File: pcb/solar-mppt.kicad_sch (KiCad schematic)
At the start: 2 parts, among them U1 BQ25798, U2 STM32G491KEUx

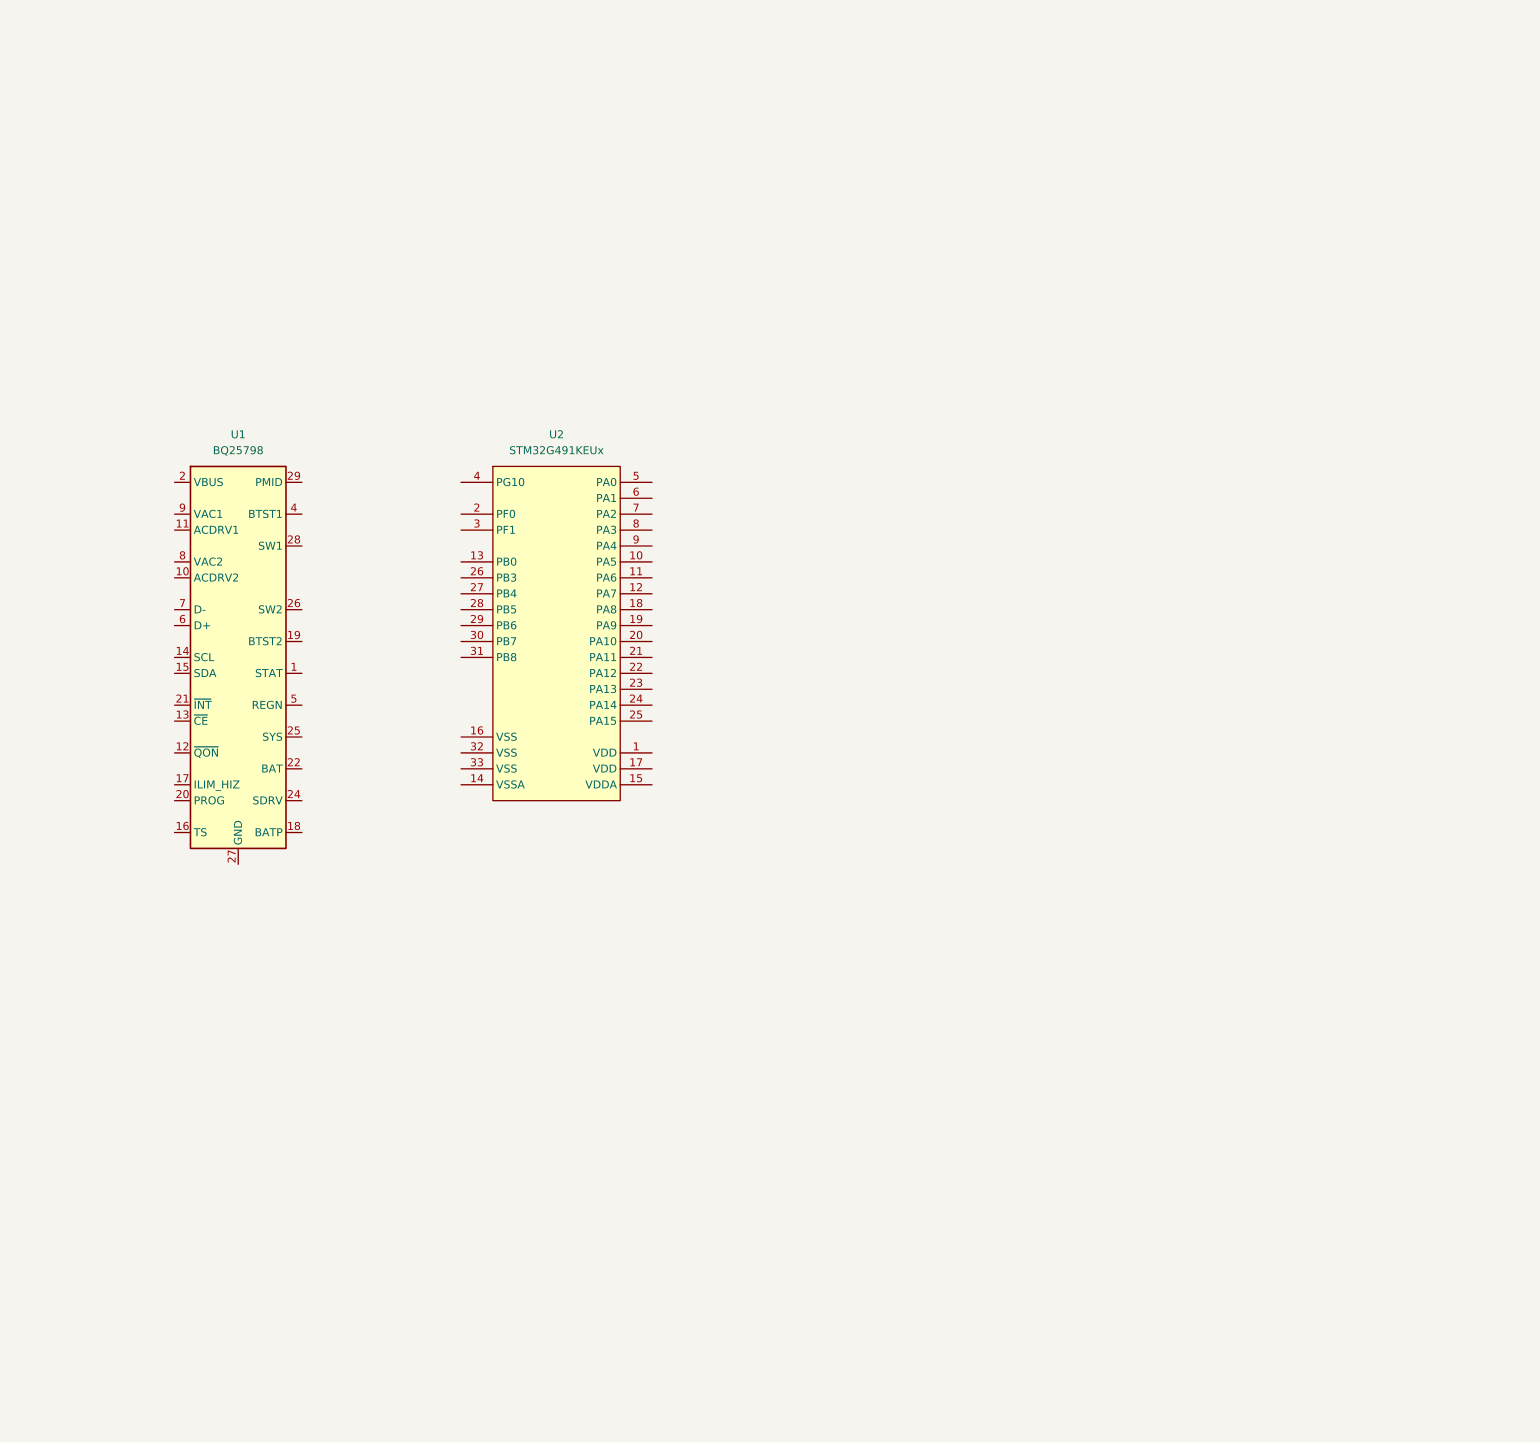
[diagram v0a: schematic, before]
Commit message: mppt vac/acdrv/vbus reverse protection b2b nmos
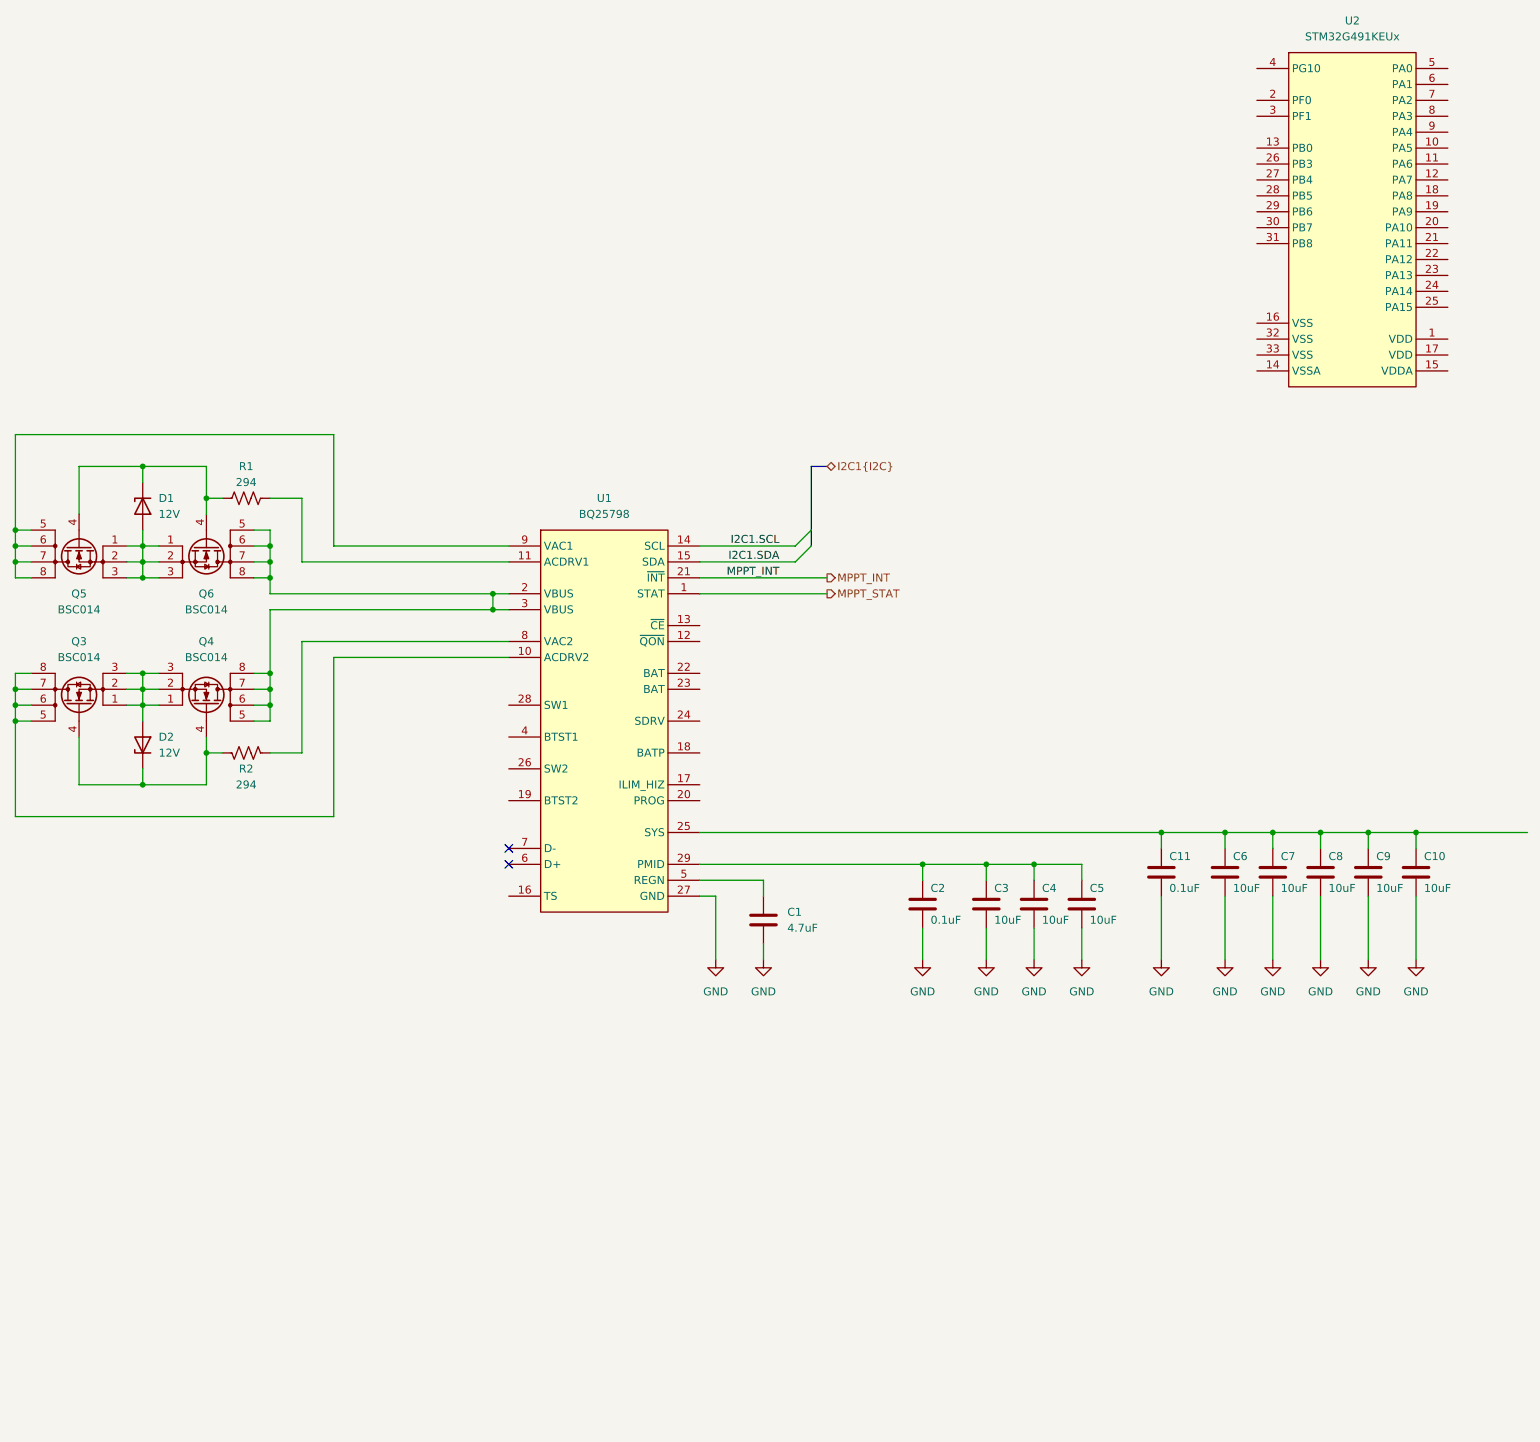
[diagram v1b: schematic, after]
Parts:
- added C1: 4.7uF, Capacitor_SMD:C_0402_1005Metric, symbol Device:C
- added C10, C3, C4, C5, C6, C7, C8, C9: 10uF, Capacitor_SMD:C_0402_1005Metric, symbol Device:C
- added C11, C2: 0.1uF, Capacitor_SMD:C_0402_1005Metric, symbol Device:C
- added D1, D2: 12V, symbol Device:D_Zener
- added Q3, Q4, Q5, Q6: BSC014, symbol Transistor_FET:Q_NMOS_DGS
- added R1, R2: 294, Resistor_SMD:R_0402_1005Metric, symbol Device:R_US
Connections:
- net MPPT_STAT: now reaches U1.1 (STAT)
- net at U1.10 (ACDRV2): now also Q3.5 (D), Q3.6 (D), Q3.7 (D), Q3.8 (D)
- net at U1.11 (ACDRV1): now also R1.2
- net I2C1.SCL: now reaches U1.14 (SCL)
- net I2C1.SDA: now reaches U1.15 (SDA)
- net at U1.2 (VBUS), U1.3 (VBUS): now also Q4.5 (D), Q4.6 (D), Q4.7 (D), Q4.8 (D), Q6.5 (D), Q6.6 (D), Q6.7 (D), Q6.8 (D)
- net MPPT_INT: now reaches U1.21 (~{INT})
- net at U1.22 (BAT): no longer U1.23 (BAT)
- net at U1.25 (SYS): now also C10.1, C11.1, C6.1, C7.1, C8.1, C9.1
- net GND: now reaches U1.27 (GND)
- net GND: now also C1.2, C10.2, C11.2, C2.2, C3.2, C4.2, C5.2, C6.2, C7.2, C8.2, C9.2
- net at U1.29 (PMID): now also C2.1, C3.1, C4.1, C5.1
- net at U1.5 (REGN): now also C1.1
- net at U1.8 (VAC2): now also R2.2
- net at U1.9 (VAC1): now also Q5.5 (D), Q5.6 (D), Q5.7 (D), Q5.8 (D)
- new net: D1.2 (A), Q5.1 (S), Q5.2 (S), Q5.3 (S), Q6.1 (S), Q6.2 (S), Q6.3 (S)
- new net: D1.1 (K), Q5.4 (G), Q6.4 (G), R1.1
- new net: D2.2 (A), Q3.1 (S), Q3.2 (S), Q3.3 (S), Q4.1 (S), Q4.2 (S), Q4.3 (S)
- new net: D2.1 (K), Q3.4 (G), Q4.4 (G), R2.1
- no-connect marks 0 -> 2
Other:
- moved on the sheet: U2

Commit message: hierarchy for mppt, label def for stm32
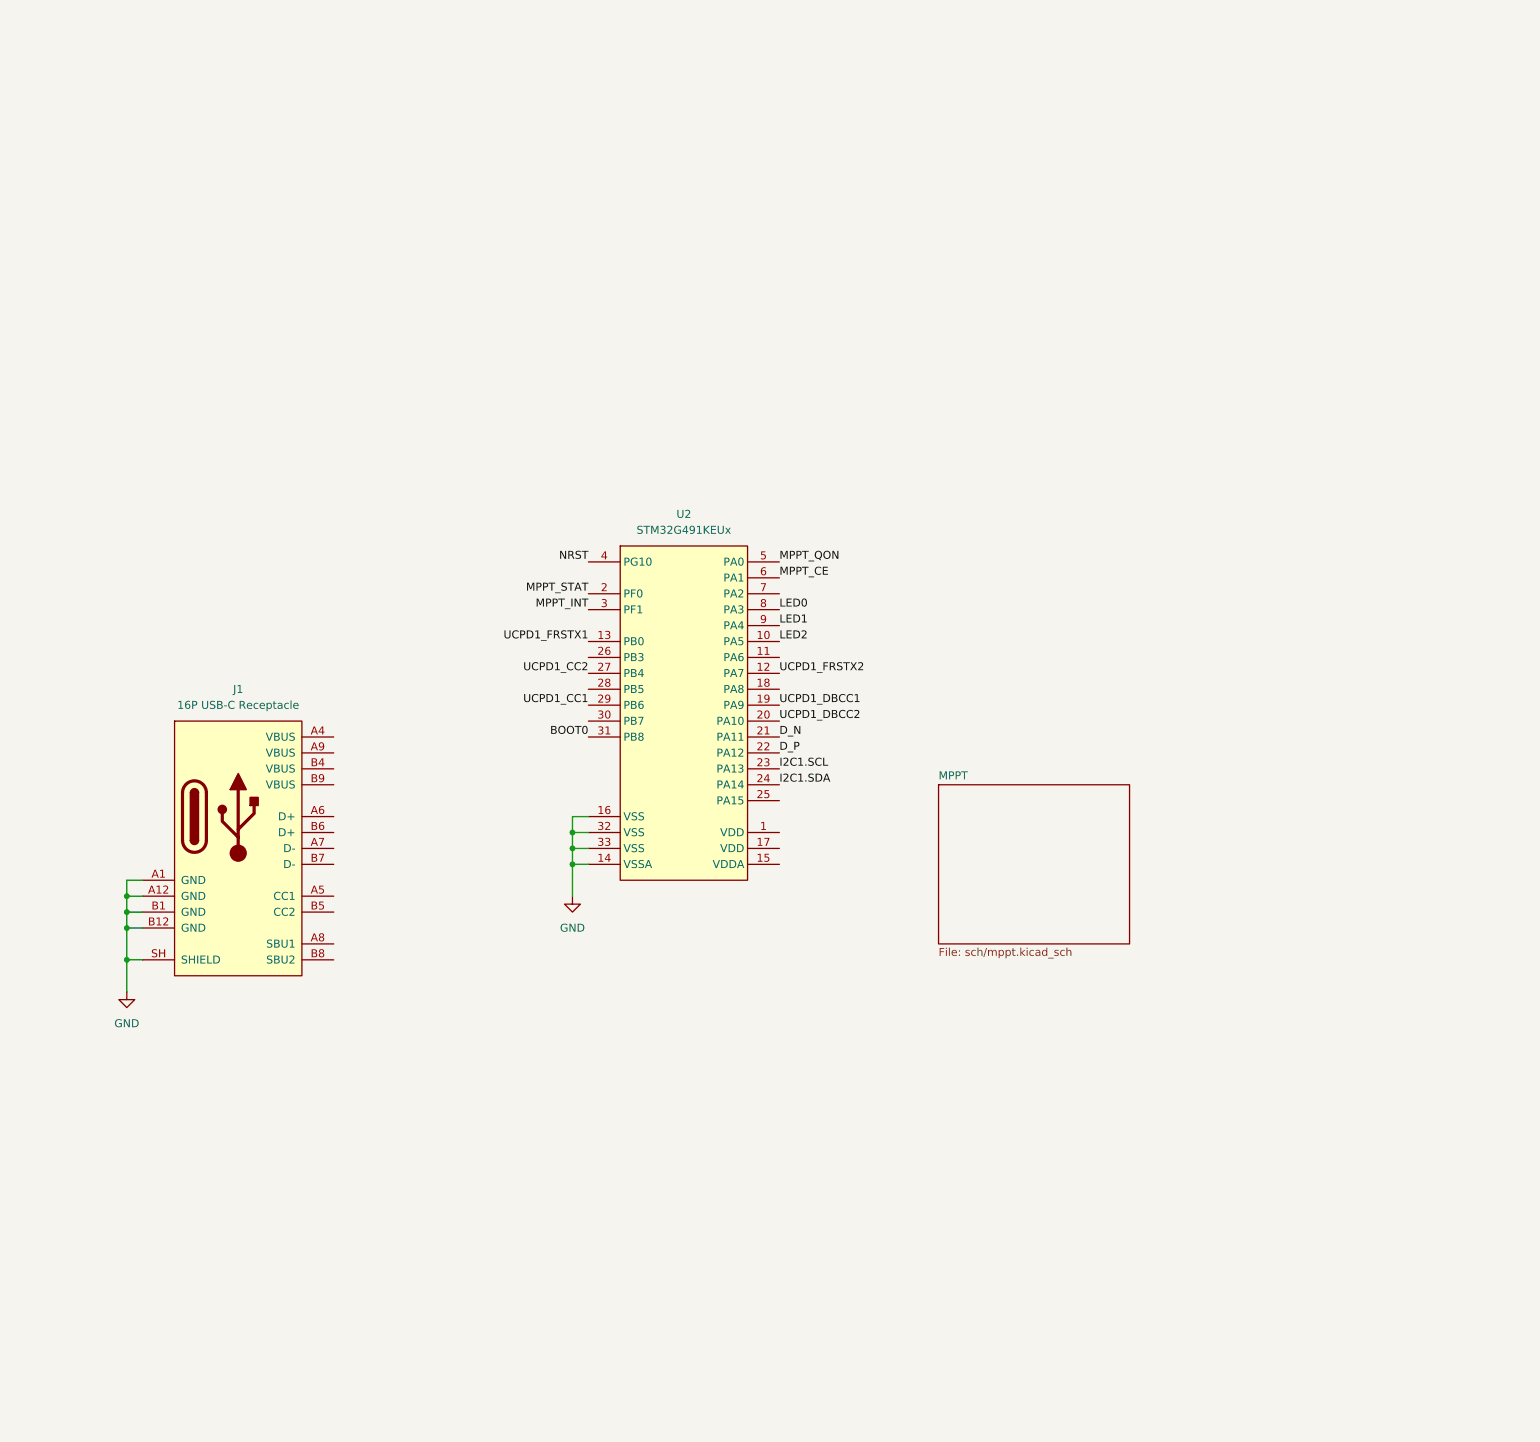
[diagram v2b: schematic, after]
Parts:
- removed C1: 4.7uF, Capacitor_SMD:C_0402_1005Metric, symbol Device:C
- removed C10, C3, C4, C5, C6, C7, C8, C9: 10uF, Capacitor_SMD:C_0402_1005Metric, symbol Device:C
- removed C11, C2: 0.1uF, Capacitor_SMD:C_0402_1005Metric, symbol Device:C
- removed D1, D2: 12V, symbol Device:D_Zener
- removed Q3, Q4, Q5, Q6: BSC014, symbol Transistor_FET:Q_NMOS_DGS
- removed R1, R2: 294, Resistor_SMD:R_0402_1005Metric, symbol Device:R_US
- removed U1: BQ25798, Package_DFN_QFN:Texas_RQM0029A_VQFN-29_4x4mm_P0.4mm, symbol Battery_Management:BQ25798
- added J1: 16P USB-C Receptacle, Connector_USB:USB_C_Receptacle_GCT_USB4105-xx-A_16P_TopMnt_Horizontal, symbol Connector:USB_C_Receptacle_USB2.0_16P
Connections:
- net GND: now also U2.14 (VSSA), U2.16 (VSS), U2.32 (VSS), U2.33 (VSS), J1.A1 (GND), J1.A12 (GND), J1.B1 (GND), J1.B12 (GND), J1.SH (SHIELD)
- net I2C1.SCL: now also U2.23 (PA13)
- net I2C1.SDA: now also U2.24 (PA14)
- net MPPT_INT: now also U2.3 (PF1)
- net MPPT_STAT: now also U2.2 (PF0)
- net LED2: now reaches U2.10 (PA5)
- net UCPD1_FRSTX2: now reaches U2.12 (PA7)
- net UCPD1_FRSTX1: now reaches U2.13 (PB0)
- net UCPD1_DBCC1: now reaches U2.19 (PA9)
- net UCPD1_DBCC2: now reaches U2.20 (PA10)
- net D_N: now reaches U2.21 (PA11)
- net D_P: now reaches U2.22 (PA12)
- net UCPD1_CC2: now reaches U2.27 (PB4)
- net UCPD1_CC1: now reaches U2.29 (PB6)
- net BOOT0: now reaches U2.31 (PB8)
- net NRST: now reaches U2.4 (PG10)
- net MPPT_QON: now reaches U2.5 (PA0)
- net MPPT_CE: now reaches U2.6 (PA1)
- net LED0: now reaches U2.8 (PA3)
- net LED1: now reaches U2.9 (PA4)
- no-connect marks 2 -> 0
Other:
- added sheet MPPT (sch/mppt.kicad_sch)
- moved on the sheet: U2

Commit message: add mcu hierarchy, rgb led, stm32 pinouts
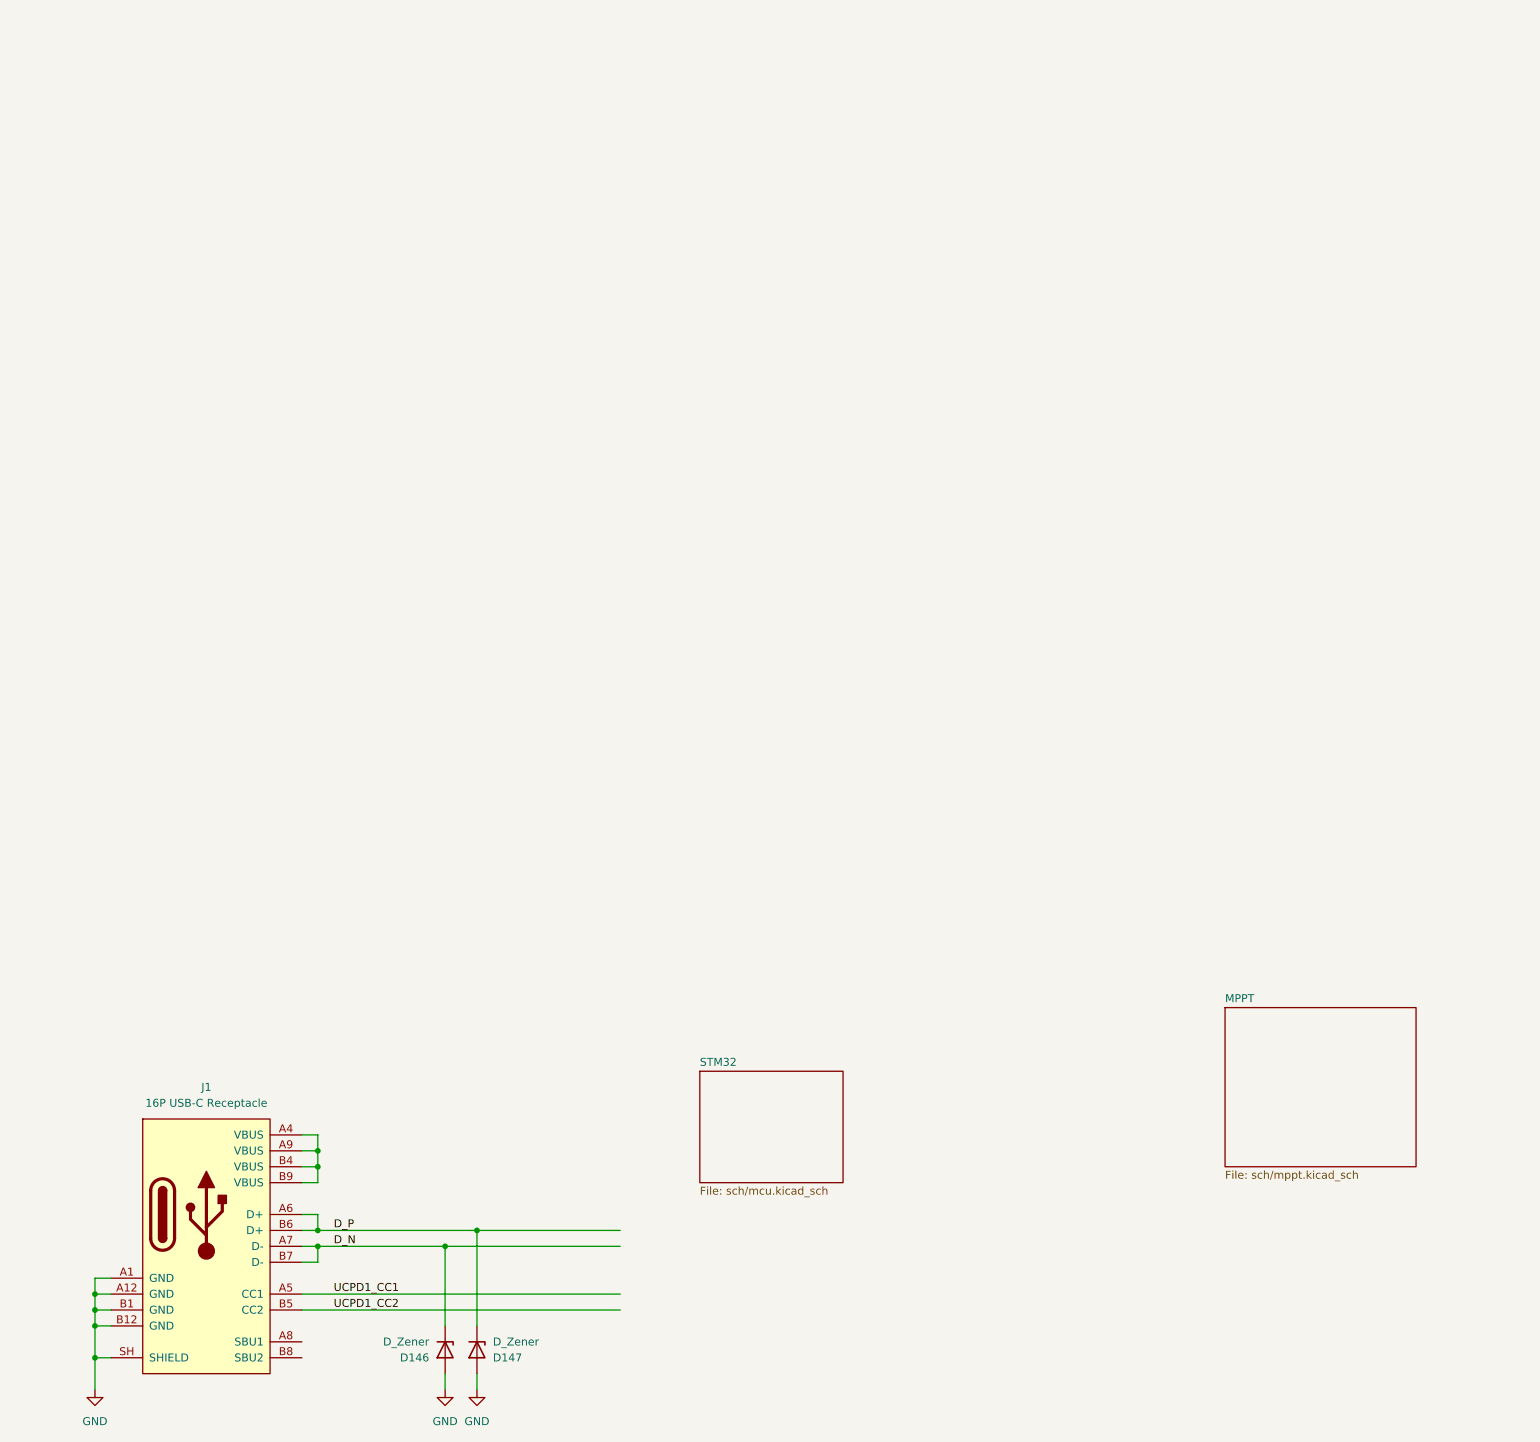
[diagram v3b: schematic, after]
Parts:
- removed U2: STM32G491KEUx, Package_DFN_QFN:QFN-32-1EP_5x5mm_P0.5mm_EP3.45x3.45mm, symbol MCU_ST_STM32G4:STM32G491KEUx
- added D146, D147: D_Zener, Diode_SMD:D_SOD-882, symbol Device:D_Zener
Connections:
- net D_N: now also J1.A7 (D-), J1.B7 (D-), D146.1 (K)
- net D_P: now also J1.A6 (D+), J1.B6 (D+), D147.1 (K)
- net GND: now also D146.2 (A), D147.2 (A)
- net UCPD1_CC1: now also J1.A5 (CC1)
- net UCPD1_CC2: now also J1.B5 (CC2)
- net at J1.A4 (VBUS): now also J1.A9 (VBUS), J1.B4 (VBUS), J1.B9 (VBUS)
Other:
- added sheet STM32 (sch/mcu.kicad_sch)
- moved on the sheet: J1
